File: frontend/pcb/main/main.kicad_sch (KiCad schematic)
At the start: 27 parts, among them J1 Ext, J2 Conn_01x02, J3 Conn_01x09, J4 Debug, J5 RS485, Q1 MMBT3904, Q2 MMBT3904, U1 ESP32-WROOM-32, U2 AP1117-33, U3 MAX485E

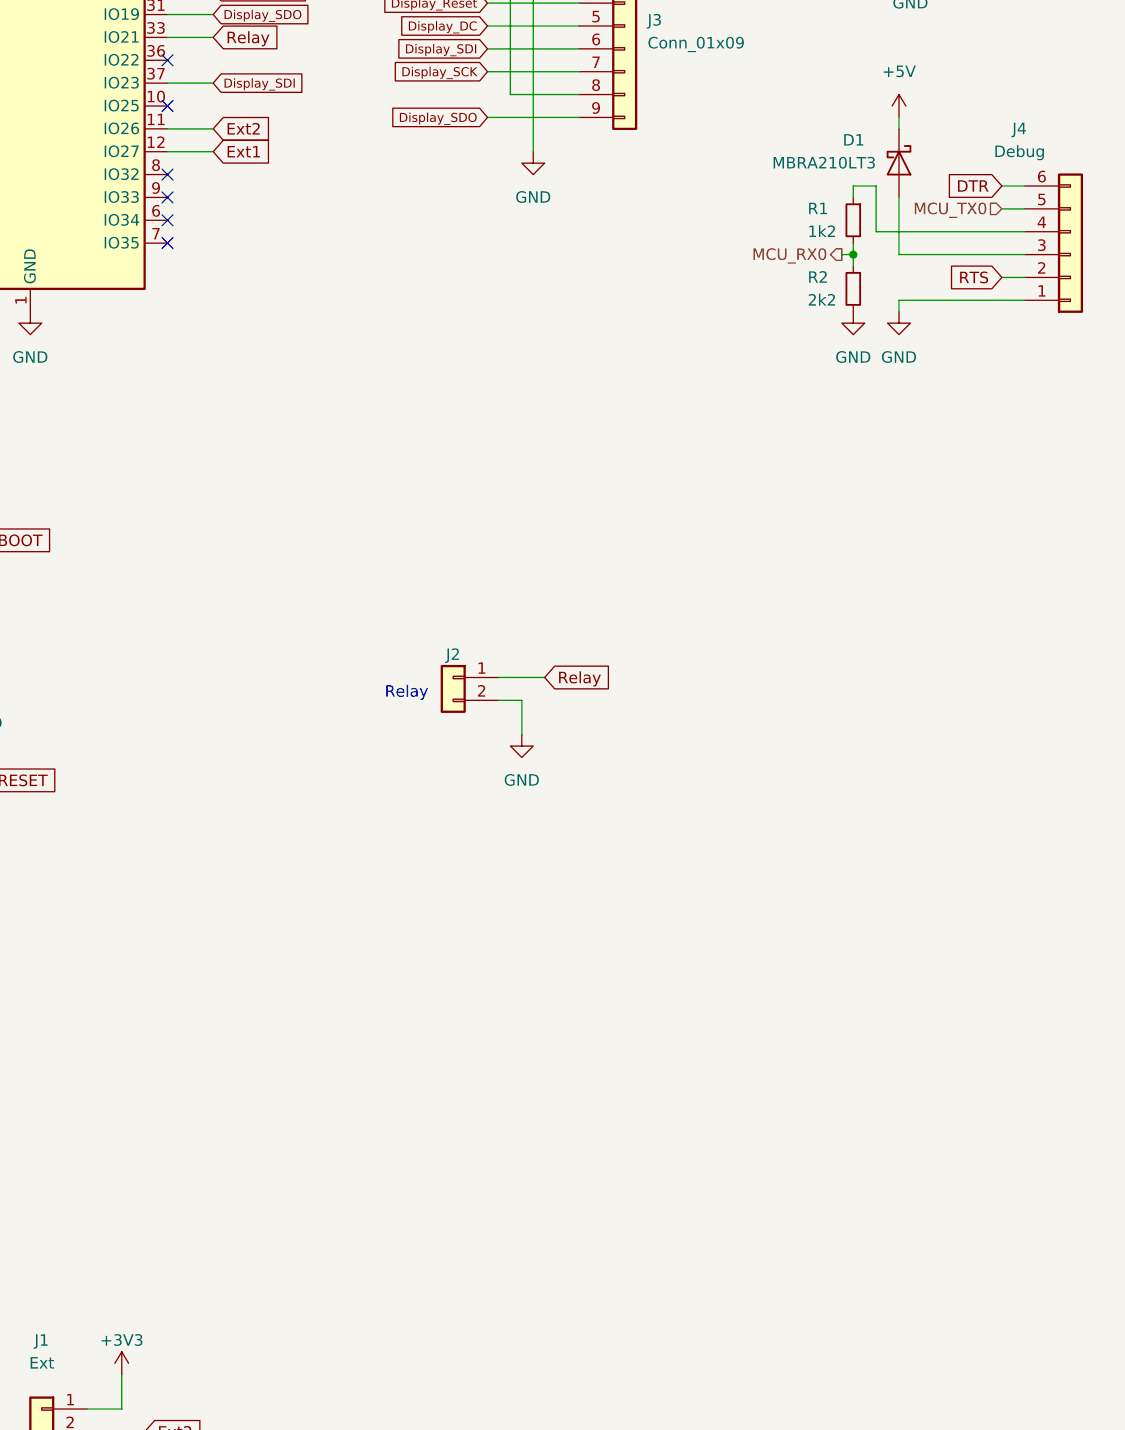
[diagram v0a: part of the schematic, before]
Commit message: Add buttons.
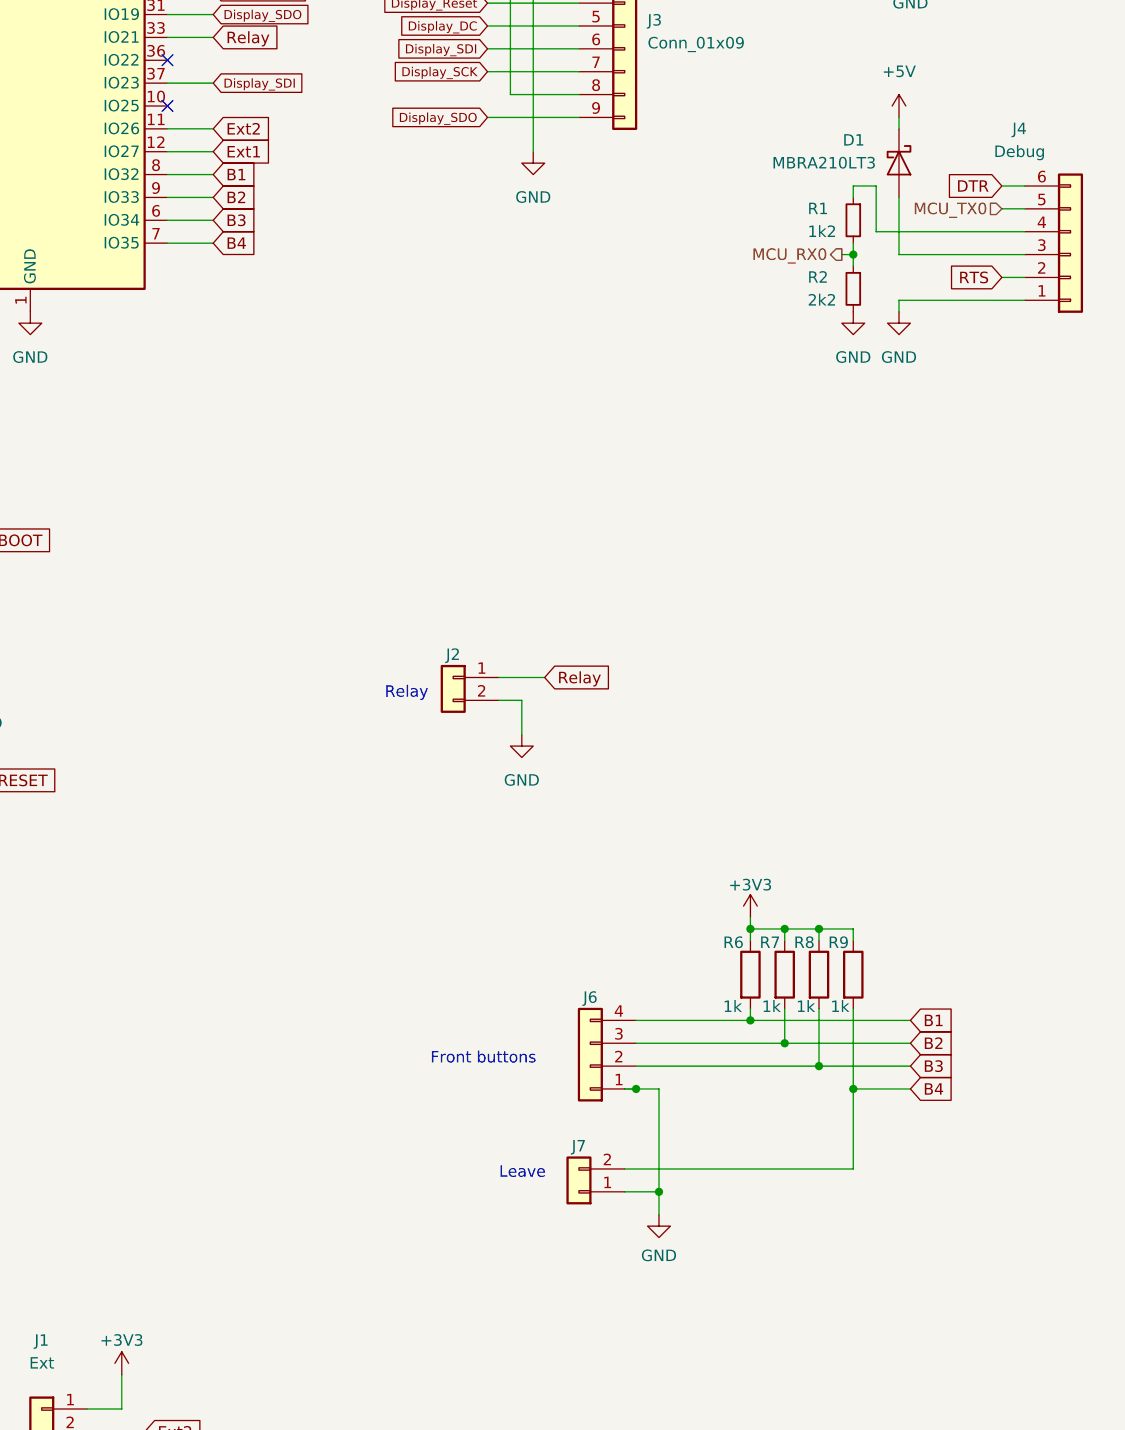
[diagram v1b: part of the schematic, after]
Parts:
- added J6: Conn_01x04, Connector_JST:JST_XH_B4B-XH-A_1x04_P2.50mm_Vertical, symbol Connector_Generic:Conn_01x04
- added J7: Conn_01x02, Connector_JST:JST_XH_B2B-XH-A_1x02_P2.50mm_Vertical, symbol Connector_Generic:Conn_01x02
- added R6, R7, R8, R9: 1k, Resistor_SMD:R_0603_1608Metric, symbol Device:R
- J4: footprint Connector_JST:JST_XH_B6B-XH-A_1x06_P2.50mm_Vertical -> Connector_PinHeader_2.54mm:PinHeader_1x06_P2.54mm_Vertical
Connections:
- net +3V3: now also R6.1, R7.1, R8.1, R9.1
- net GND: now also J6.1 (Pin_1), J7.1 (Pin_1)
- net B3: now reaches U1.6 (IO34)
- net B3: now also J6.2 (Pin_2), R8.2
- net B4: now reaches U1.7 (IO35)
- net B4: now also J7.2 (Pin_2), R9.2
- net B1: now reaches U1.8 (IO32)
- net B1: now also J6.4 (Pin_4), R6.2
- net B2: now reaches U1.9 (IO33)
- net B2: now also J6.3 (Pin_3), R7.2
- no-connect marks 17 -> 13
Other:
- note added: "Front buttons"
- note added: "Leave"

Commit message: Finish relay board.
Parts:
- removed J2: Conn_01x02, Connector_JST:JST_XH_B2B-XH-A_1x02_P2.50mm_Vertical, symbol Connector_Generic:Conn_01x02
- added J2: Conn_01x03, Connector_PinHeader_2.54mm:PinHeader_1x03_P2.54mm_Vertical, symbol Connector_Generic:Conn_01x03
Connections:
- net +5V: now also J2.3 (Pin_3)
- net B1: now also U1.6 (IO34); no longer U1.8 (IO32)
- net B2: now also U1.7 (IO35); no longer U1.9 (IO33)
- net B3: now also U1.8 (IO32); no longer U1.6 (IO34)
- net B4: now also U1.9 (IO33); no longer U1.7 (IO35)
- net GND: now also J2.1 (Pin_1)
- net Relay: now also J2.2 (Pin_2)
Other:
- note added: "To relay PCB"
- note removed: "Relay"
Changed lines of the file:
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@@
+    (stroke (width 0) (type default))
+  )
+  (wire (pts (xy 232.41 146.05) (xy 232.41 149.86))
     (stroke (width 0) (type default))
   )
@@
     (stroke (width 0) (type default))
   )
+  (wire (pts (xy 232.41 137.16) (xy 232.41 140.97))
+    (stroke (width 0) (type default))
+  )
   (wire (pts (xy 153.67 173.99) (xy 171.45 173.99))
     (stroke (width 0) (type default))
@@
     (stroke (width 0) (type default))
   )
-  (wire (pts (xy 125.73 138.43) (xy 128.27 138.43))
-    (stroke (width 0) (type default))
-  )
   (wire (pts (xy 25.4 173.99) (xy 25.4 177.8))
     (stroke (width 0) (type default))
@@
     (stroke (width 0) (type default))
   )
-  (wire (pts (xy 128.27 138.43) (xy 128.27 142.24))
-    (stroke (width 0) (type default))
-  )
   (wire (pts (xy 88.9 46.99) (xy 93.98 46.99))
     (stroke (width 0) (type default))
   )
-  (wire (pts (xy 125.73 135.89) (xy 130.81 135.89))
-    (stroke (width 0) (type default))
-  )
   (wire (pts (xy 181.61 44.45) (xy 181.61 45.72))
     (stroke (width 0) (type default))
@@
     (stroke (width 0) (type default))
   )
+  (wire (pts (xy 232.41 143.51) (xy 236.22 143.51))
+    (stroke (width 0) (type default))
+  )
   (wire (pts (xy 58.42 147.32) (xy 68.58 147.32))
     (stroke (width 0) (type default))
@@
     (stroke (width 0) (type default))
   )
+  (wire (pts (xy 232.41 140.97) (xy 236.22 140.97))
+    (stroke (width 0) (type default))
+  )
   (wire (pts (xy 171.45 181.61) (xy 165.1 181.61))
     (stroke (width 0) (type default))
@@
     (stroke (width 0) (type default))
   )
+  (wire (pts (xy 236.22 146.05) (xy 232.41 146.05))
+    (stroke (width 0) (type default))
+  )
   (wire (pts (xy 281.94 69.85) (xy 281.94 71.12))
     (stroke (width 0) (type default))
@@
   (wire (pts (xy 88.9 31.75) (xy 91.44 31.75))
     (stroke (width 0) (type default))
-  )
-  (text "Relay" (exclude_from_sim no)
- (at 113.03 138.43 0)
-    (effects (font (size 1.27 1.27)) (justify left bottom))
   )
   (text "MSP4020" (exclude_from_sim no)
@@
     (effects (font (size 1.27 1.27)) (justify left bottom))
   )
-  (global_label "B2" (shape input) (at 93.98 82.55 0) (fields_autoplaced)
-    (effects (font (size 1.27 1.27)) (justify left))
-    (property "Intersheetrefs" "${INTERSHEET_REFS}" (at 99.3653 82.55 0)
+  (text "To relay PCB" (exclude_from_sim no)
+ (at 243.84 140.97 0)
+    (effects (font (size 1.27 1.27)) (justify left bottom))
+  )
+  (global_label "B2" (shape input) (at 93.98 87.63 0) (fields_autoplaced)
+    (effects (font (size 1.27 1.27)) (justify left))
+    (property "Intersheetrefs" "${INTERSHEET_REFS}" (at 99.3653 87.63 0)
       (effects (font (size 1.27 1.27)) (justify left) hide)
     )
@@
     )
   )
-  (global_label "B4" (shape input) (at 93.98 87.63 0) (fields_autoplaced)
-    (effects (font (size 1.27 1.27)) (justify left))
-    (property "Intersheetrefs" "${INTERSHEET_REFS}" (at 99.3653 87.63 0)
+  (global_label "B4" (shape input) (at 93.98 82.55 0) (fields_autoplaced)
+    (effects (font (size 1.27 1.27)) (justify left))
+    (property "Intersheetrefs" "${INTERSHEET_REFS}" (at 99.3653 82.55 0)
       (effects (font (size 1.27 1.27)) (justify left) hide)
     )
@@
     )
   )
-  (global_label "B3" (shape input) (at 93.98 85.09 0) (fields_autoplaced)
+  (global_label "B3" (shape input) (at 93.98 80.01 0) (fields_autoplaced)
+    (effects (font (size 1.27 1.27)) (justify left))
+    (property "Intersheetrefs" "${INTERSHEET_REFS}" (at 99.3653 80.01 0)
+      (effects (font (size 1.27 1.27)) (justify left) hide)
+    )
+  )
+  (global_label "B1" (shape input) (at 93.98 85.09 0) (fields_autoplaced)
     (effects (font (size 1.27 1.27)) (justify left))
     (property "Intersheetrefs" "${INTERSHEET_REFS}" (at 99.3653 85.09 0)
-      (effects (font (size 1.27 1.27)) (justify left) hide)
-    )
-  )
-  (global_label "B1" (shape input) (at 93.98 80.01 0) (fields_autoplaced)
-    (effects (font (size 1.27 1.27)) (justify left))
-    (property "Intersheetrefs" "${INTERSHEET_REFS}" (at 99.3653 80.01 0)
       (effects (font (size 1.27 1.27)) (justify left) hide)
     )
@@
     )
   )
-  (global_label "Relay" (shape input) (at 130.81 135.89 0) (fields_autoplaced)
-    (effects (font (size 1.27 1.27)) (justify left))
-    (property "Intersheetrefs" "${INTERSHEET_REFS}" (at 138.8562 135.89 0)
-      (effects (font (size 1.27 1.27)) (justify left) hide)
-    )
-  )
   (global_label "BOOT" (shape input) (at 91.44 29.21 0) (fields_autoplaced)
     (effects (font (size 1.27 1.27)) (justify left))
@@
     (property "Intersheetrefs" "${INTERSHEET_REFS}" (at 176.5331 178.9906 0)
       (effects (font (size 1.27 1.27)) (justify left) hide)
+    )
+  )
+  (global_label "Relay" (shape input) (at 232.41 143.51 180) (fields_autoplaced)
+    (effects (font (size 1.27 1.27)) (justify right))
+    (property "Intersheetrefs" "${INTERSHEET_REFS}" (at 224.3638 143.51 0)
+      (effects (font (size 1.27 1.27)) (justify right) hide)
     )
   )
@@
     )
   )
-  (symbol (lib_id "Connector_Generic:Conn_01x02") (at 120.65 135.89 0) (mirror y) (unit 1)
-    (in_bom yes) (on_board yes) (dnp no) (fields_autoplaced)
-    (property "Reference" "J2" (at 120.65 133.35 0)
-      (effects (font (size 1.27 1.27)))
-    )
-    (property "Value" "Conn_01x02" (at 120.65 133.35 0)
-      (effects (font (size 1.27 1.27)) hide)
-    )
-    (property "Footprint" "Connector_JST:JST_XH_B2B-XH-A_1x02_P2.50mm_Vertical" (at 120.65 135.89 0)
-      (effects (font (size 1.27 1.27)) hide)
-    )
-    (property "Datasheet" "~" (at 120.65 135.89 0)
-      (effects (font (size 1.27 1.27)) hide)
-    )
-    (pin "1")
-    (pin "2")
+  (symbol (lib_id "Connector_Generic:Conn_01x03") (at 241.3 143.51 0) (mirror x) (unit 1)
+    (in_bom yes) (on_board yes) (dnp no)
+    (property "Reference" "J2" (at 243.84 144.145 0)
+      (effects (font (size 1.27 1.27)) (justify left))
+    )
+    (property "Value" "Conn_01x03" (at 243.84 141.605 0)
+      (effects (font (size 1.27 1.27)) (justify left) hide)
+    )
+    (property "Footprint" "Connector_PinHeader_2.54mm:PinHeader_1x03_P2.54mm_Vertical" (at 241.3 143.51 0)
+      (effects (font (size 1.27 1.27)) hide)
+    )
+    (property "Datasheet" "~" (at 241.3 143.51 0)
+      (effects (font (size 1.27 1.27)) hide)
+    )
+    (pin "1")
+    (pin "2")
+    (pin "3")
     (instances
       (project "main"
@@
     )
   )
-  (symbol (lib_id "power:GND") (at 128.27 142.24 0) (unit 1)
-    (in_bom yes) (on_board yes) (dnp no) (fields_autoplaced)
-    (property "Reference" "#PWR010" (at 128.27 148.59 0)
-      (effects (font (size 1.27 1.27)) hide)
-    )
-    (property "Value" "GND" (at 128.27 147.32 0)
-      (effects (font (size 1.27 1.27)))
-    )
-    (property "Footprint" "" (at 128.27 142.24 0)
-      (effects (font (size 1.27 1.27)) hide)
-    )
-    (property "Datasheet" "" (at 128.27 142.24 0)
-      (effects (font (size 1.27 1.27)) hide)
-    )
-    (pin "1")
-    (instances
-      (project "main"
-        (path "/212a0d71-cc7b-49f8-b4ca-a935e5355dca"
-          (reference "#PWR010") (unit 1)
-        )
-      )
-    )
-  )
   (symbol (lib_id "power:+3V3") (at 33.02 33.02 0) (unit 1)
     (in_bom yes) (on_board yes) (dnp no) (fields_autoplaced)
@@
         (path "/218f1b12-ca06-4253-bcd5-950f07f2eb16"
           (reference "R9") (unit 1)
+        )
+      )
+    )
+  )
+  (symbol (lib_id "power:GND") (at 232.41 149.86 0) (unit 1)
+    (in_bom yes) (on_board yes) (dnp no) (fields_autoplaced)
+    (property "Reference" "#PWR025" (at 232.41 156.21 0)
+      (effects (font (size 1.27 1.27)) hide)
+    )
+    (property "Value" "GND" (at 232.41 154.94 0)
+      (effects (font (size 1.27 1.27)))
+    )
+    (property "Footprint" "" (at 232.41 149.86 0)
+      (effects (font (size 1.27 1.27)) hide)
+    )
+    (property "Datasheet" "" (at 232.41 149.86 0)
+      (effects (font (size 1.27 1.27)) hide)
+    )
+    (pin "1")
+    (instances
+      (project "main"
+        (path "/212a0d71-cc7b-49f8-b4ca-a935e5355dca"
+          (reference "#PWR025") (unit 1)
         )
       )
@@
         )
       )
+    )
+  )
+  (symbol (lib_id "power:+5V") (at 232.41 137.16 0) (unit 1)
+    (in_bom yes) (on_board yes) (dnp no) (fields_autoplaced)
+    (property "Reference" "#PWR024" (at 232.41 140.97 0)
+      (effects (font (size 1.27 1.27)) hide)
+    )
+    (property "Value" "+5V" (at 232.41 133.35 0)
+      (effects (font (size 1.27 1.27)))
+    )
+    (property "Footprint" "" (at 232.41 137.16 0)
+      (effects (font (size 1.27 1.27)) hide)
+    )
+    (property "Datasheet" "" (at 232.41 137.16 0)
+      (effects (font (size 1.27 1.27)) hide)
+    )
+    (pin "1")
+    (instances
+      (project "main"
+        (path "/212a0d71-cc7b-49f8-b4ca-a935e5355dca"
+          (reference "#PWR024") (unit 1)
+        )
+      )

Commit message: Remove capacitors.
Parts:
- removed C2, C3: 100n, Capacitor_SMD:C_0603_1608Metric, symbol Device:C
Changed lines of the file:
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@@
   (junction (at 161.29 179.07) (diameter 0) (color 0 0 0 0)
   )
-  (junction (at 58.42 133.35) (diameter 0) (color 0 0 0 0)
-  )
-  (junction (at 58.42 147.32) (diameter 0) (color 0 0 0 0)
-  )
   (junction (at 143.51 193.04) (diameter 0) (color 0 0 0 0)
   )
@@
   )
   (junction (at 171.45 54.61) (diameter 0) (color 0 0 0 0)
-  )
-  (junction (at 58.42 120.65) (diameter 0) (color 0 0 0 0)
   )
   (junction (at 165.1 88.9) (diameter 0) (color 0 0 0 0)
@@
   (no_connect (at 88.9 57.15))
   (no_connect (at 88.9 44.45))
-  (wire (pts (xy 58.42 120.65) (xy 68.58 120.65))
+  (wire (pts (xy 46.99 120.65) (xy 68.58 120.65))
     (stroke (width 0) (type default))
   )
@@
     (stroke (width 0) (type default))
   )
-  (wire (pts (xy 68.58 133.35) (xy 58.42 133.35))
-    (stroke (width 0) (type default))
-  )
-  (wire (pts (xy 58.42 144.78) (xy 58.42 147.32))
-    (stroke (width 0) (type default))
-  )
   (wire (pts (xy 88.9 62.23) (xy 93.98 62.23))
     (stroke (width 0) (type default))
@@
     (stroke (width 0) (type default))
   )
-  (wire (pts (xy 58.42 120.65) (xy 58.42 123.19))
-    (stroke (width 0) (type default))
-  )
   (wire (pts (xy 242.57 41.91) (xy 242.57 53.34))
     (stroke (width 0) (type default))
@@
     (stroke (width 0) (type default))
   )
-  (wire (pts (xy 58.42 130.81) (xy 58.42 133.35))
-    (stroke (width 0) (type default))
-  )
   (wire (pts (xy 134.62 55.88) (xy 129.54 55.88))
     (stroke (width 0) (type default))
@@
     (stroke (width 0) (type default))
   )
-  (wire (pts (xy 46.99 147.32) (xy 58.42 147.32))
+  (wire (pts (xy 46.99 147.32) (xy 68.58 147.32))
     (stroke (width 0) (type default))
   )
@@
     (stroke (width 0) (type default))
   )
-  (wire (pts (xy 46.99 120.65) (xy 58.42 120.65))
-    (stroke (width 0) (type default))
-  )
   (wire (pts (xy 170.18 73.66) (xy 170.18 74.93))
     (stroke (width 0) (type default))
@@
     (stroke (width 0) (type default))
   )
-  (wire (pts (xy 58.42 133.35) (xy 58.42 137.16))
-    (stroke (width 0) (type default))
-  )
   (wire (pts (xy 232.41 143.51) (xy 236.22 143.51))
     (stroke (width 0) (type default))
   )
-  (wire (pts (xy 58.42 147.32) (xy 68.58 147.32))
-    (stroke (width 0) (type default))
-  )
   (wire (pts (xy 161.29 179.07) (xy 171.45 179.07))
     (stroke (width 0) (type default))
@@
   )
   (wire (pts (xy 153.67 163.83) (xy 157.48 163.83))
-    (stroke (width 0) (type default))
-  )
-  (wire (pts (xy 68.58 135.89) (xy 68.58 133.35))
     (stroke (width 0) (type default))
   )
@@
         (path "/212a0d71-cc7b-49f8-b4ca-a935e5355dca"
           (reference "#PWR011") (unit 1)
-        )
-      )
-    )
-  )
-  (symbol (lib_name "C_2") (lib_id "Device:C") (at 58.42 140.97 0) (unit 1)
-    (in_bom yes) (on_board yes) (dnp no) (fields_autoplaced)
-    (property "Reference" "C3" (at 62.23 140.335 0)
-      (effects (font (size 1.27 1.27)) (justify left))
-    )
-    (property "Value" "100n" (at 62.23 142.875 0)
-      (effects (font (size 1.27 1.27)) (justify left))
-    )
-    (property "Footprint" "Capacitor_SMD:C_0603_1608Metric" (at 59.3852 144.78 0)
-      (effects (font (size 1.27 1.27)) hide)
-    )
-    (property "Datasheet" "~" (at 58.42 140.97 0)
-      (effects (font (size 1.27 1.27)) hide)
-    )
-    (pin "1")
-    (pin "2")
-    (instances
-      (project "main"
-        (path "/212a0d71-cc7b-49f8-b4ca-a935e5355dca"
-          (reference "C3") (unit 1)
-        )
-      )
-      (project "reader"
-        (path "/218f1b12-ca06-4253-bcd5-950f07f2eb16"
-          (reference "C3") (unit 1)
         )
       )
@@
     )
   )
-  (symbol (lib_name "GND_3") (lib_id "power:GND") (at 68.58 135.89 0) (unit 1)
-    (in_bom yes) (on_board yes) (dnp no) (fields_autoplaced)
-    (property "Reference" "#PWR04" (at 68.58 142.24 0)
-      (effects (font (size 1.27 1.27)) hide)
-    )
-    (property "Value" "GND" (at 68.58 140.97 0)
-      (effects (font (size 1.27 1.27)))
-    )
-    (property "Footprint" "" (at 68.58 135.89 0)
-      (effects (font (size 1.27 1.27)) hide)
-    )
-    (property "Datasheet" "" (at 68.58 135.89 0)
-      (effects (font (size 1.27 1.27)) hide)
-    )
-    (pin "1")
-    (instances
-      (project "main"
-        (path "/212a0d71-cc7b-49f8-b4ca-a935e5355dca"
-          (reference "#PWR04") (unit 1)
-        )
-      )
-      (project "reader"
-        (path "/218f1b12-ca06-4253-bcd5-950f07f2eb16"
-          (reference "#PWR010") (unit 1)
-        )
-      )
-    )
-  )
   (symbol (lib_id "Regulator_Linear:AP1117-33") (at 171.45 45.72 0) (unit 1)
     (in_bom yes) (on_board yes) (dnp no) (fields_autoplaced)
@@
         )
       )
-    )
-  )
-  (symbol (lib_name "C_3") (lib_id "Device:C") (at 58.42 127 0) (unit 1)
-    (in_bom yes) (on_board yes) (dnp no) (fields_autoplaced)
-    (property "Reference" "C2" (at 62.23 126.365 0)
-      (effects (font (size 1.27 1.27)) (justify left))
-    )
-    (property "Value" "100n" (at 62.23 128.905 0)
-      (effects (font (size 1.27 1.27)) (justify left))
-    )
-    (property "Footprint" "Capacitor_SMD:C_0603_1608Metric" (at 59.3852 130.81 0)
-      (effects (font (size 1.27 1.27)) hide)
-    )
-    (property "Datasheet" "~" (at 58.42 127 0)
-      (effects (font (size 1.27 1.27)) hide)
-    )
-    (pin "1")
-    (pin "2")
-    (instances
-      (project "main"
-        (path "/212a0d71-cc7b-49f8-b4ca-a935e5355dca"
-          (reference "C2") (unit 1)
-        )
-      )
-      (project "reader"
-        (path "/218f1b12-ca06-4253-bcd5-950f07f2eb16"
-          (reference "C6") (unit 1)
-        )
-      )
